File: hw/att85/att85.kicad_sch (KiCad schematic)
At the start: 43 parts, among them J101 Barrel_Jack_Switch, J102 Screw_Terminal_01x03, J103 AVR-ISP-6, J104 Conn_01x02, J105 Conn_01x02, Q101 BC817, SW101 SW_Push, SW102 SW_Push, SW103 SW_Push, SW104 SW_Push, SW105 SW_Push, SW106 SW_Push, U101 ATtiny85-20P, U102 MT3608-MODULE, U105 74AHC1G125

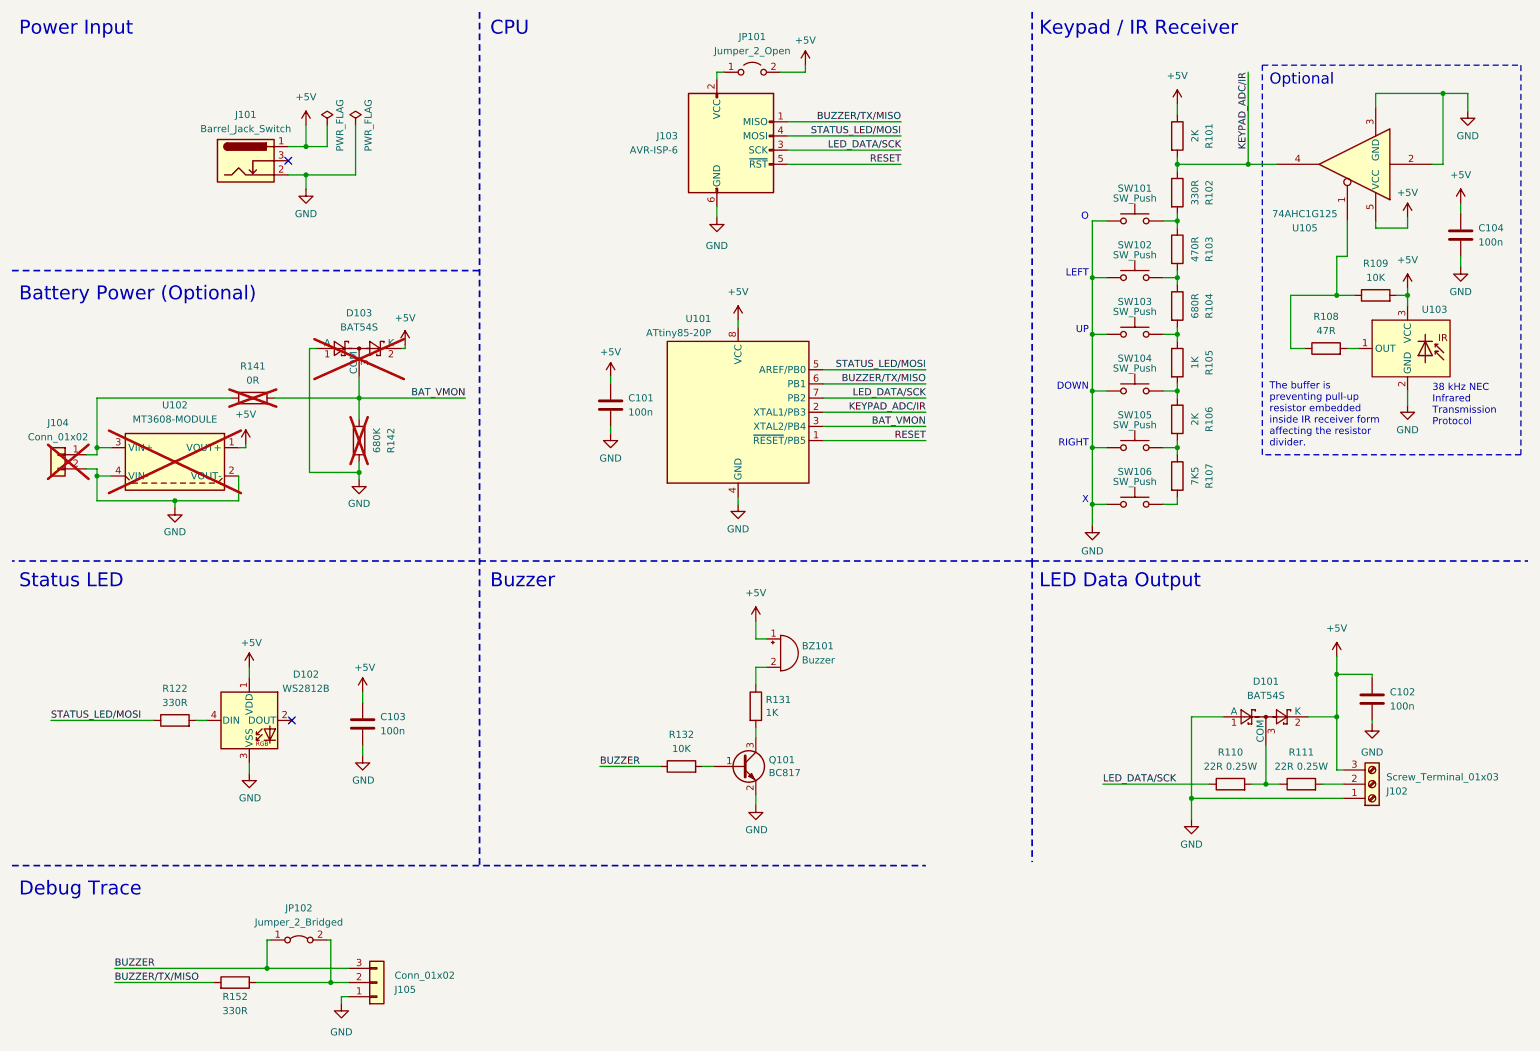
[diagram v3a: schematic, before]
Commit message: chore(hw): move status LED on main LED DATA, use freed pin for RX
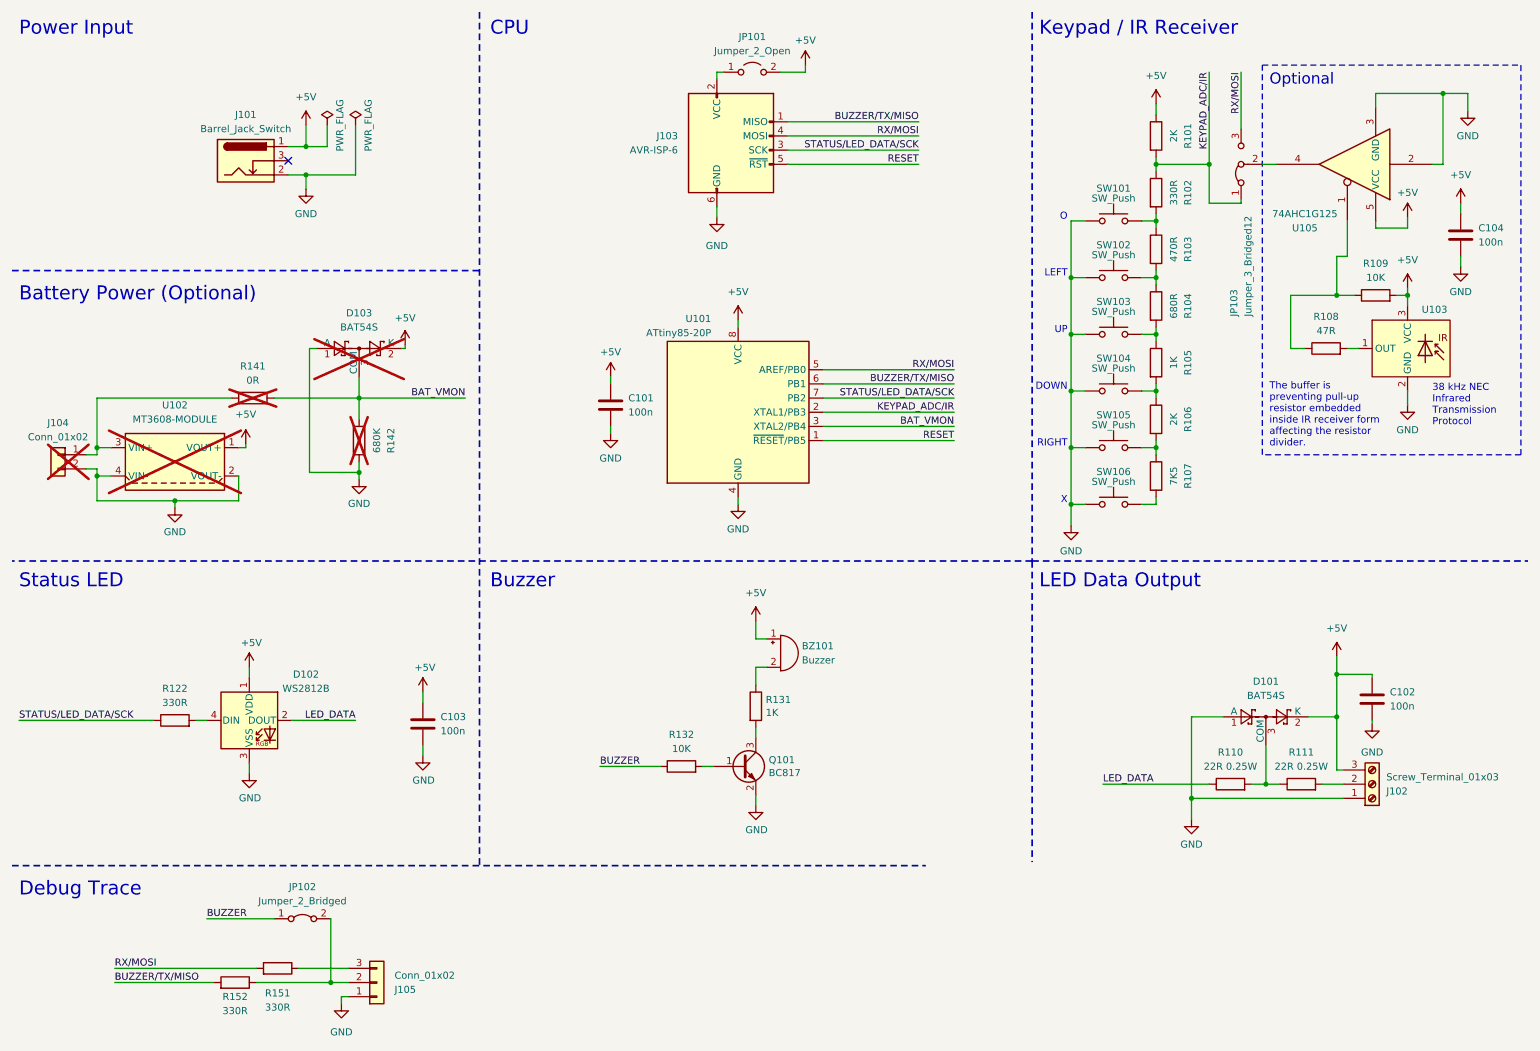
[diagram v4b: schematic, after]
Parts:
- added JP103: Jumper_3_Bridged12, Jumper:SolderJumper-3_P1.3mm_Bridged12_RoundedPad1.0x1.5mm, symbol Jumper:Jumper_3_Bridged12
- added R151: 330R, Resistor_SMD:R_0805_2012Metric_Pad1.20x1.40mm_HandSolder, symbol Device:R
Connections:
- net BUZZER: no longer J105.3 (Pin_3)
- net KEYPAD_ADC/IR: now also JP103.1 (A); no longer U105.4
- net LED_DATA: now reaches D102.2 (DOUT)
- net LED_DATA: now also R110.1
- net LED_DATA/SCK renamed STATUS/LED_DATA/SCK
- net STATUS/LED_DATA/SCK: now also R122.1; no longer R110.1
- net STATUS_LED/MOSI renamed RX/MOSI
- net RX/MOSI: now also JP103.3 (B), R151.2; no longer R122.1
- new net: JP103.2 (C), U105.4
- new net: J105.3 (Pin_3), R151.1
- no-connect marks 2 -> 1
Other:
- moved on the sheet: C103, JP102, R101, R102, R103, R104, R105, R106, R107, SW101, SW102, SW103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

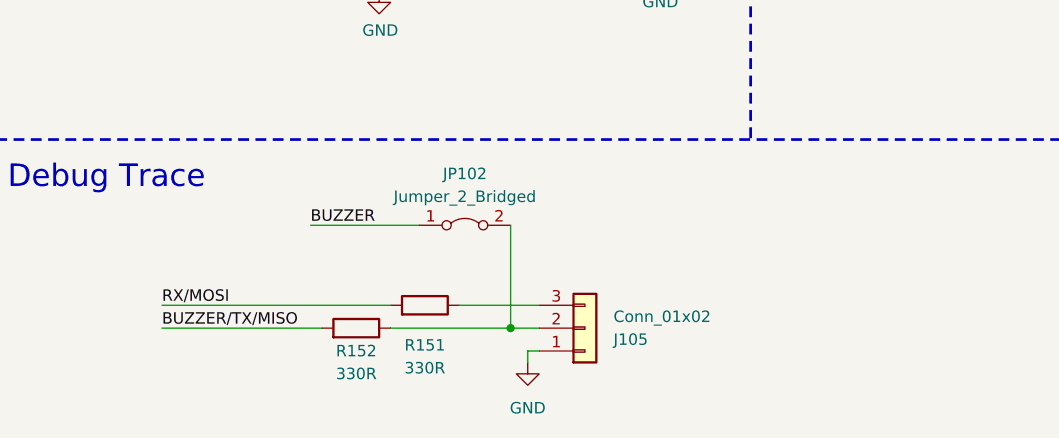
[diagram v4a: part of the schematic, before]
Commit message: chore(hw): move buzzer connection, update layout
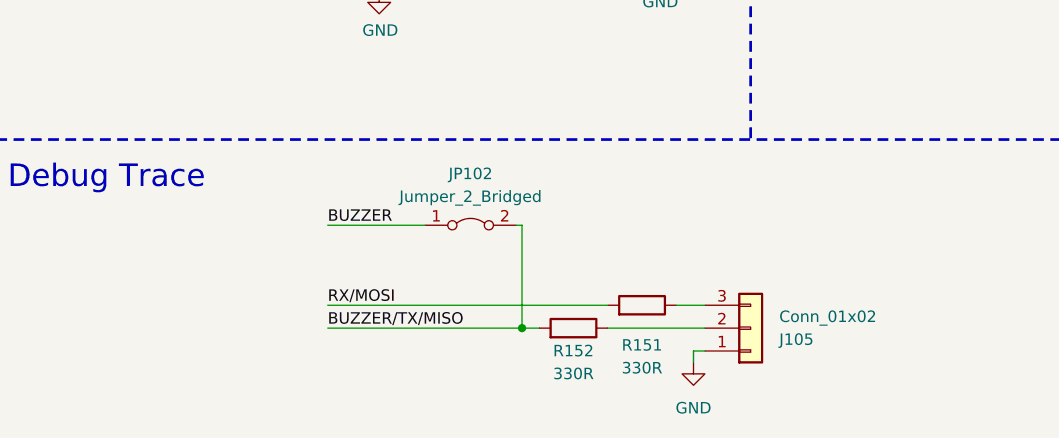
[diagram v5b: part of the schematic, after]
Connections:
- net BUZZER/TX/MISO: now also JP102.2 (B)
- net at J105.2 (Pin_2), R152.1: no longer JP102.2 (B)
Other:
- moved on the sheet: J105, JP102, R151, R152
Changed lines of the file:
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@@
     (comment 1 "www.stefanmisik.com")
   )
-  (junction (at 69.85 186.69) (diameter 0) (color 0 0 0 0)
+  (junction (at 71.12 186.69) (diameter 0) (color 0 0 0 0)
   )
   (junction (at 237.49 151.13) (diameter 0) (color 0 0 0 0)
@@
     (stroke (width 0) (type default))
   )
-  (wire (pts (xy 69.85 175.26) (xy 69.85 186.69))
-    (stroke (width 0) (type default))
-  )
   (wire (pts (xy 245.11 139.065) (xy 250.19 139.065))
     (stroke (width 0) (type default))
@@
     (stroke (width 0) (type default))
   )
-  (wire (pts (xy 71.755 189.23) (xy 73.025 189.23))
-    (stroke (width 0) (type default))
-  )
-  (wire (pts (xy 69.85 186.69) (xy 73.025 186.69))
+  (wire (pts (xy 90.17 189.23) (xy 91.44 189.23))
+    (stroke (width 0) (type default))
+  )
+  (wire (pts (xy 80.645 186.69) (xy 91.44 186.69))
     (stroke (width 0) (type default))
   )
@@
     (stroke (width 0) (type default))
   )
+  (wire (pts (xy 71.12 186.69) (xy 73.025 186.69))
+    (stroke (width 0) (type default))
+  )
   (wire (pts (xy 217.805 69.215) (xy 217.805 70.485))
     (stroke (width 0) (type default))
@@
     (stroke (width 0) (type default))
   )
-  (wire (pts (xy 56.515 186.69) (xy 69.85 186.69))
-    (stroke (width 0) (type default))
-  )
   (wire (pts (xy 233.045 23.495) (xy 233.045 33.655))
     (stroke (width 0) (type default))
@@
     (stroke (width 0) (type default))
   )
-  (wire (pts (xy 31.115 184.15) (xy 56.515 184.15))
+  (wire (pts (xy 49.53 184.15) (xy 80.645 184.15))
     (stroke (width 0) (type default))
   )
@@
     (stroke (width 0) (type default))
   )
-  (wire (pts (xy 31.115 186.69) (xy 48.895 186.69))
-    (stroke (width 0) (type default))
-  )
   (wire (pts (xy 256.54 132.08) (xy 256.54 131.445))
+    (stroke (width 0) (type default))
+  )
+  (wire (pts (xy 71.12 175.26) (xy 71.12 186.69))
     (stroke (width 0) (type default))
   )
@@
     (stroke (width 0.3) (type dash))
   )
-  (wire (pts (xy 71.755 190.5) (xy 71.755 189.23))
+  (wire (pts (xy 90.17 190.5) (xy 90.17 189.23))
     (stroke (width 0) (type default))
   )
@@
     (stroke (width 0) (type default))
   )
-  (wire (pts (xy 64.135 184.15) (xy 73.025 184.15))
+  (wire (pts (xy 88.265 184.15) (xy 91.44 184.15))
     (stroke (width 0) (type default))
   )
@@
     (stroke (width 0) (type default))
   )
+  (wire (pts (xy 70.485 175.26) (xy 71.12 175.26))
+    (stroke (width 0) (type default))
+  )
   (wire (pts (xy 86.36 134.62) (xy 86.36 136.525))
     (stroke (width 0) (type default))
@@
   )
   (wire (pts (xy 83.185 73.025) (xy 82.55 73.025))
+    (stroke (width 0) (type default))
+  )
+  (wire (pts (xy 49.53 186.69) (xy 71.12 186.69))
     (stroke (width 0) (type default))
   )
@@
     (stroke (width 0) (type default))
   )
-  (wire (pts (xy 47.625 175.26) (xy 59.69 175.26))
+  (wire (pts (xy 49.53 175.26) (xy 60.325 175.26))
     (stroke (width 0) (type default))
   )
@@
     (effects (font (size 1.27 1.27)) (justify right bottom))
   )
-  (label "BUZZER{slash}TX{slash}MISO" (at 31.115 186.69 0) (fields_autoplaced)
+  (label "BUZZER{slash}TX{slash}MISO" (at 49.53 186.69 0) (fields_autoplaced)
     (effects (font (size 1.27 1.27)) (justify left bottom))
   )
@@
     (effects (font (size 1.27 1.27)) (justify right bottom))
   )
-  (label "BUZZER" (at 47.625 175.26 0) (fields_autoplaced)
+  (label "BUZZER" (at 49.53 175.26 0) (fields_autoplaced)
     (effects (font (size 1.27 1.27)) (justify left bottom))
   )
@@
     (effects (font (size 1.27 1.27)) (justify left bottom))
   )
-  (label "RX{slash}MOSI" (at 31.115 184.15 0) (fields_autoplaced)
+  (label "RX{slash}MOSI" (at 49.53 184.15 0) (fields_autoplaced)
     (effects (font (size 1.27 1.27)) (justify left bottom))
   )
@@
     )
   )
-  (symbol (lib_id "Device:R") (at 60.325 184.15 270) (mirror x) (unit 1)
-    (in_bom yes) (on_board yes) (dnp no)
-    (property "Reference" "R151" (at 60.325 188.595 90)
-      (effects (font (size 1.27 1.27)))
-    )
-    (property "Value" "330R" (at 60.325 191.135 90)
-      (effects (font (size 1.27 1.27)))
-    )
-    (property "Footprint" "Resistor_SMD:R_0805_2012Metric_Pad1.20x1.40mm_HandSolder" (at 60.325 185.928 90)
-      (effects (font (size 1.27 1.27)) hide)
-    )
-    (property "Datasheet" "~" (at 60.325 184.15 0)
+  (symbol (lib_id "Device:R") (at 84.455 184.15 270) (mirror x) (unit 1)
+    (in_bom yes) (on_board yes) (dnp no)
+    (property "Reference" "R151" (at 84.455 188.595 90)
+      (effects (font (size 1.27 1.27)))
+    )
+    (property "Value" "330R" (at 84.455 191.135 90)
+      (effects (font (size 1.27 1.27)))
+    )
+    (property "Footprint" "Resistor_SMD:R_0805_2012Metric_Pad1.20x1.40mm_HandSolder" (at 84.455 185.928 90)
+      (effects (font (size 1.27 1.27)) hide)
+    )
+    (property "Datasheet" "~" (at 84.455 184.15 0)
       (effects (font (size 1.27 1.27)) hide)
     )
@@
     )
   )
-  (symbol (lib_id "Connector_Generic:Conn_01x03") (at 78.105 186.69 0) (mirror x) (unit 1)
-    (in_bom yes) (on_board yes) (dnp no)
-    (property "Reference" "J105" (at 81.28 187.96 0)
+  (symbol (lib_id "Connector_Generic:Conn_01x03") (at 96.52 186.69 0) (mirror x) (unit 1)
+    (in_bom yes) (on_board yes) (dnp no)
+    (property "Reference" "J105" (at 99.695 187.96 0)
       (effects (font (size 1.27 1.27)) (justify left))
     )
-    (property "Value" "Conn_01x02" (at 81.28 185.42 0)
+    (property "Value" "Conn_01x02" (at 99.695 185.42 0)
       (effects (font (size 1.27 1.27)) (justify left))
     )
-    (property "Footprint" "Connector_PinHeader_2.54mm:PinHeader_1x03_P2.54mm_Vertical" (at 78.105 186.69 0)
-      (effects (font (size 1.27 1.27)) hide)
-    )
-    (property "Datasheet" "~" (at 78.105 186.69 0)
+    (property "Footprint" "Connector_PinHeader_2.54mm:PinHeader_1x03_P2.54mm_Vertical" (at 96.52 186.69 0)
+      (effects (font (size 1.27 1.27)) hide)
+    )
+    (property "Datasheet" "~" (at 96.52 186.69 0)
       (effects (font (size 1.27 1.27)) hide)
     )
@@
     )
   )
-  (symbol (lib_id "power:GND") (at 71.755 190.5 0) (unit 1)
-    (in_bom yes) (on_board yes) (dnp no) (fields_autoplaced)
-    (property "Reference" "#PWR0121" (at 71.755 196.85 0)
-      (effects (font (size 1.27 1.27)) hide)
-    )
-    (property "Value" "GND" (at 71.755 195.58 0)
-      (effects (font (size 1.27 1.27)))
-    )
-    (property "Footprint" "" (at 71.755 190.5 0)
-      (effects (font (size 1.27 1.27)) hide)
-    )
-    (property "Datasheet" "" (at 71.755 190.5 0)
+  (symbol (lib_id "power:GND") (at 90.17 190.5 0) (unit 1)
+    (in_bom yes) (on_board yes) (dnp no) (fields_autoplaced)
+    (property "Reference" "#PWR0121" (at 90.17 196.85 0)
+      (effects (font (size 1.27 1.27)) hide)
+    )
+    (property "Value" "GND" (at 90.17 195.58 0)
+      (effects (font (size 1.27 1.27)))
+    )
+    (property "Footprint" "" (at 90.17 190.5 0)
+      (effects (font (size 1.27 1.27)) hide)
+    )
+    (property "Datasheet" "" (at 90.17 190.5 0)
       (effects (font (size 1.27 1.27)) hide)
     )
@@
     )
   )
-  (symbol (lib_id "Device:R") (at 52.705 186.69 270) (mirror x) (unit 1)
-    (in_bom yes) (on_board yes) (dnp no)
-    (property "Reference" "R152" (at 52.705 189.23 90)
-      (effects (font (size 1.27 1.27)))
-    )
-    (property "Value" "330R" (at 52.705 191.77 90)
-      (effects (font (size 1.27 1.27)))
-    )
-    (property "Footprint" "Resistor_SMD:R_0805_2012Metric_Pad1.20x1.40mm_HandSolder" (at 52.705 188.468 90)
-      (effects (font (size 1.27 1.27)) hide)
-    )
-    (property "Datasheet" "~" (at 52.705 186.69 0)
+  (symbol (lib_id "Device:R") (at 76.835 186.69 270) (mirror x) (unit 1)
+    (in_bom yes) (on_board yes) (dnp no)
+    (property "Reference" "R152" (at 76.835 189.23 90)
+      (effects (font (size 1.27 1.27)))
+    )
+    (property "Value" "330R" (at 76.835 191.77 90)
+      (effects (font (size 1.27 1.27)))
+    )
+    (property "Footprint" "Resistor_SMD:R_0805_2012Metric_Pad1.20x1.40mm_HandSolder" (at 76.835 188.468 90)
+      (effects (font (size 1.27 1.27)) hide)
+    )
+    (property "Datasheet" "~" (at 76.835 186.69 0)
       (effects (font (size 1.27 1.27)) hide)
     )
@@
     )
   )
-  (symbol (lib_id "Jumper:Jumper_2_Bridged") (at 64.77 175.26 0) (unit 1)
-    (in_bom yes) (on_board yes) (dnp no) (fields_autoplaced)
-    (property "Reference" "JP102" (at 64.77 169.545 0)
-      (effects (font (size 1.27 1.27)))
-    )
-    (property "Value" "Jumper_2_Bridged" (at 64.77 172.085 0)
-      (effects (font (size 1.27 1.27)))
-    )
-    (property "Footprint" "Jumper:SolderJumper-2_P1.3mm_Bridged_RoundedPad1.0x1.5mm" (at 64.77 175.26 0)
-      (effects (font (size 1.27 1.27)) hide)
-    )
-    (property "Datasheet" "~" (at 64.77 175.26 0)
-      (effects (font (size 1.27 1.27)) hide)
-    )
+  (symbol (lib_id "Jumper:Jumper_2_Bridged") (at 65.405 175.26 0) (unit 1)
+    (in_bom yes) (on_board yes) (dnp no) (fields_autoplaced)
+    (property "Reference" "JP102" (at 65.405 169.545 0)
+      (effects (font (size 1.27 1.27)))
+    )
+    (property "Value" "Jumper_2_Bridged" (at 65.405 172.085 0)
+      (effects (font (size 1.27 1.27)))
+    )
+    (property "Footprint" "Jumper:SolderJumper-2_P1.3mm_Bridged_RoundedPad1.0x1.5mm" (at 65.405 175.26 0)
+      (effects (font (size 1.27 1.27)) hide)
+    )
+    (property "Datasheet" "~" (at 65.405 175.26 0)
+      (effects (font (size 1.27 1.27)) hide)
+    )
